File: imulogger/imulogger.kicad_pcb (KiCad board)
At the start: 2 copper layers, 64 x 25 mm, 36 parts, among them J1 DEBUG, J2 BATCONN, J4 Micro_SD_Card, J5 PWRCONN, Q1 TP0610T, U1 ESP32-WROOM-32, U2 USFS, U3 MCP1826S, U4 MCP73831-2-OT, U5 dw01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

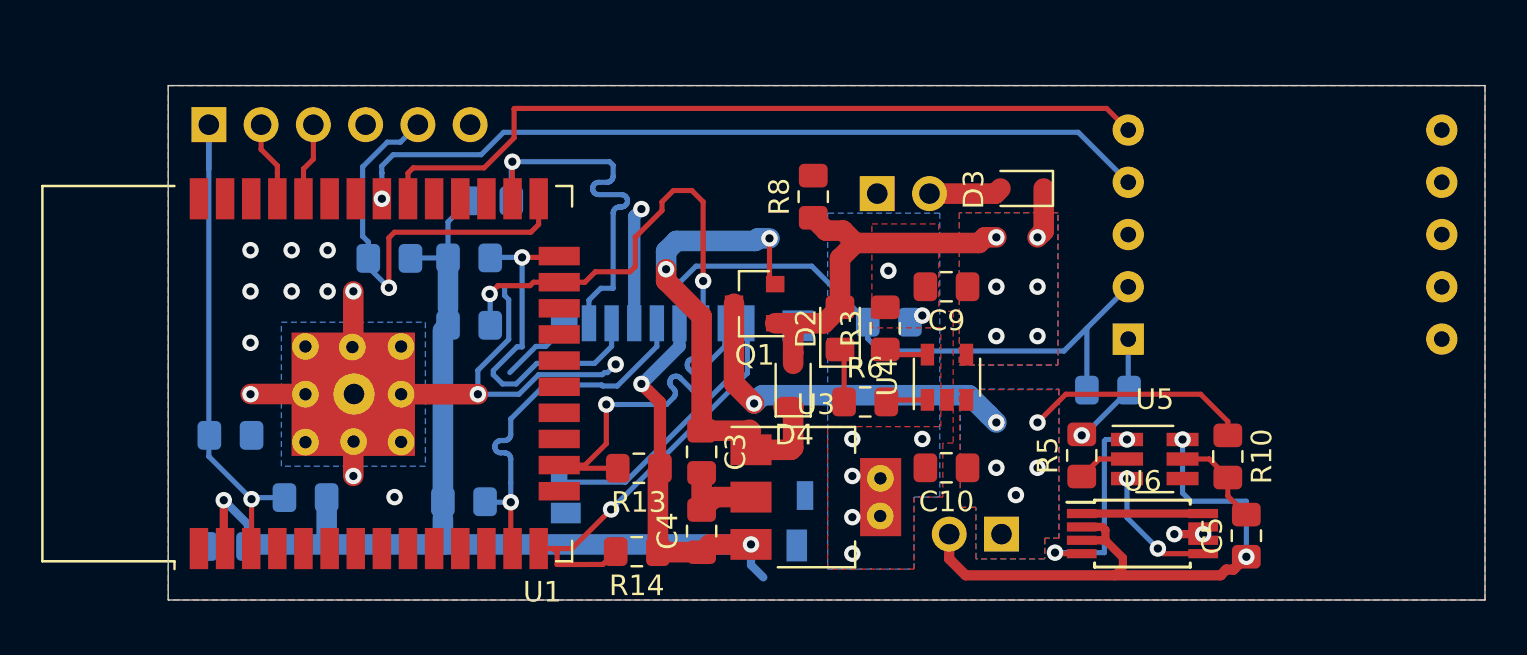
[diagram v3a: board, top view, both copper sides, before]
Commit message: imulogger: put connectors on the component side and remove useless track
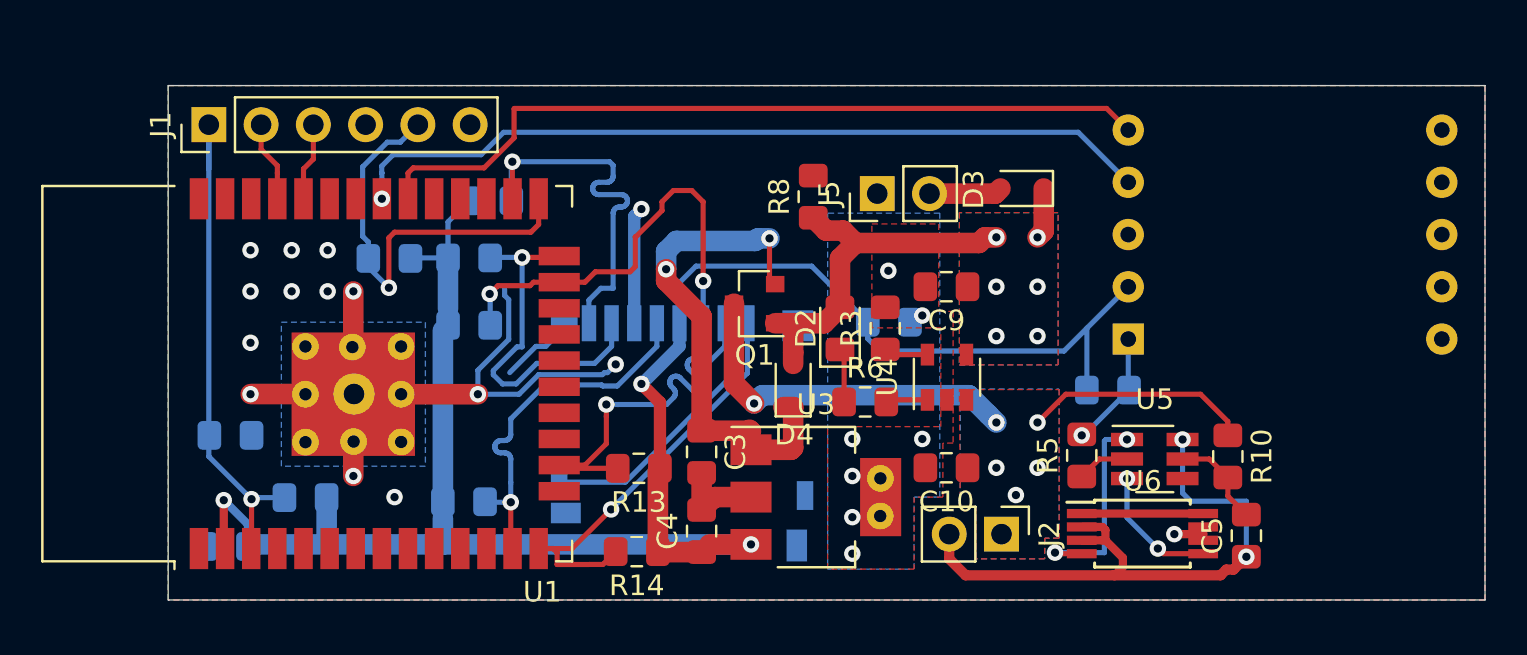
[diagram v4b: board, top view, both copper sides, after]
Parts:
- J1, J2, J5: moved to F.Cu
- turned J1 to 90 degrees
- turned J2 to 270 degrees
- turned J5 to 90 degrees
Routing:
- net +3V3: track 100.6 -> 98.8 mm
- net GND: vias 24 -> 23

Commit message: remove charger and add switch and JST socket
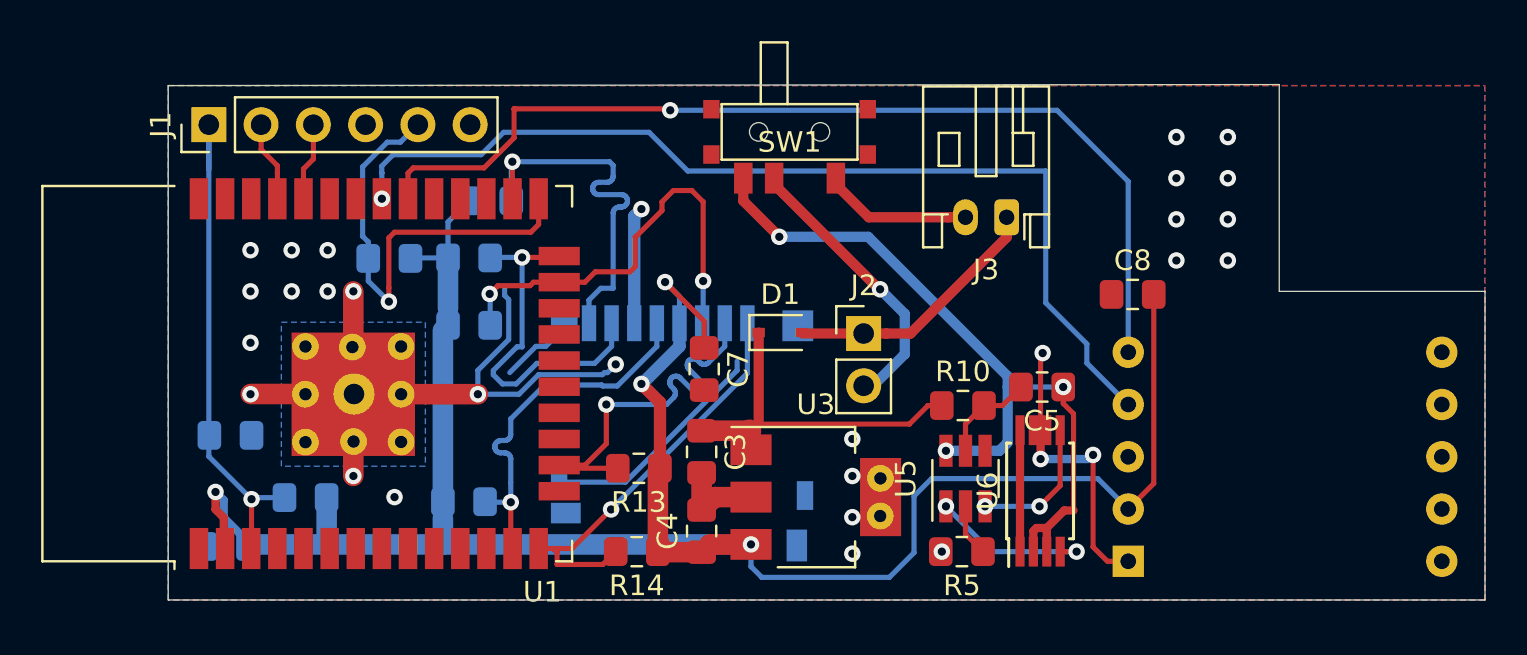
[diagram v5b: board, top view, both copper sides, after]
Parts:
- removed C10, C9: 4.7u, Capacitor_SMD:C_0805_2012Metric_Pad1.15x1.40mm_HandSolder
- removed D2: LED, LED_SMD:LED_0805_2012Metric_Pad1.15x1.40mm_HandSolder
- removed D3, D4: BAT20J, Diode_SMD:D_SOD-323
- removed J5: PWRCONN, Connector_PinHeader_2.54mm:PinHeader_1x02_P2.54mm_Vertical
- removed Q1: TP0610T, Package_TO_SOT_SMD:SOT-23
- removed R3: 2k, Resistor_SMD:R_0805_2012Metric_Pad1.15x1.40mm_HandSolder
- removed R6: 470, Resistor_SMD:R_0805_2012Metric_Pad1.15x1.40mm_HandSolder
- removed R8: 10k, Resistor_SMD:R_0805_2012Metric_Pad1.15x1.40mm_HandSolder
- removed U4: MCP73831-2-OT, Package_TO_SOT_SMD:SOT-23-5
- added D1: BAT20J, Diode_SMD:D_SOD-323, F.Cu at (149.8, 71.0)
- added J3: CHGCONN, Connector_JST:JST_PH_S2B-PH-K_1x02_P2.00mm_Horizontal, F.Cu at (160.8, 65.4)
- added SW1: SW_SPDT, imulogger-footprints:SK-3296S-01-L3, F.Cu at (150.2, 61.2)
- C7, C8: moved to F.Cu
- moved R10 13.1 mm to (158.6, 74.5), turned to 0 degrees
- moved C5 12.3 mm to (162.5, 73.7), turned to 180 degrees
- moved J2 11.8 mm to (153.8, 71.0), turned to 0 degrees
- moved U2 10.8 mm to (174.3, 77.0)
- moved C7 9.26 mm to (146.1, 72.8), turned to 270 degrees
- moved U5 9.25 mm to (158.8, 78.1), turned to 90 degrees
- moved R5 7.47 mm to (158.6, 81.7), turned to 180 degrees
- moved U6 5.39 mm to (162.4, 78.7), turned to 90 degrees
- moved C8 4.80 mm to (166.9, 69.2), turned to 0 degrees
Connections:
- C3 pad 1: Net-(C3-Pad1) -> V_BAT
- J2 pad 1: V_BAT -> Net-(D1-Pad2)
- J2 pad 2: Net-(C5-Pad1) -> Net-(J2-Pad2)
- U3 pad 1: Net-(C3-Pad1) -> V_BAT
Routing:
- net Net-(C3-Pad1): track 25.7 -> 0.00 mm, vias 2 -> 0
- net V_EXT: track 20.9 -> 0.00 mm, vias 6 -> 0
- net Net-(J2-Pad2): track 0.00 -> 13.8 mm, vias 0 -> 1
- net Net-(D1-Pad2): track 0.00 -> 12.9 mm
- net +3V3: track 98.8 -> 110.4 mm, vias 3 -> 4
- net V_BAT: track 28.8 -> 18.8 mm, vias 6 -> 0
- net IMU_SDA: track 38.8 -> 48.2 mm, vias 0 -> 1
- net IMU_SCL: track 39.6 -> 48.3 mm
- net GND: track 69.5 -> 76.7 mm, vias 23 -> 30
- net Net-(J3-Pad2): track 0.00 -> 7.26 mm
- net Net-(C5-Pad1): track 30.6 -> 37.3 mm, vias 2 -> 3
- net Net-(D3-Pad2): track 3.55 -> 0.00 mm
- net Net-(D2-Pad1): track 2.63 -> 0.00 mm
- net Net-(U5-Pad1): track 10.3 -> 8.06 mm
- net Net-(R3-Pad1): track 2.15 -> 0.00 mm
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- removed copper zone on B.Cu, net V_BAT
- removed copper zone on F.Cu, net V_BAT
- removed copper zone on B.Cu, net V_EXT
- removed copper zone on F.Cu, net V_EXT
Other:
- outline, holes or cut-outs redrawn

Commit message: remove battery protection circuit
my battery has that already and even if I had one without one
it'd be easier to buy one and glue it to the battery than soldering
these small ICs.
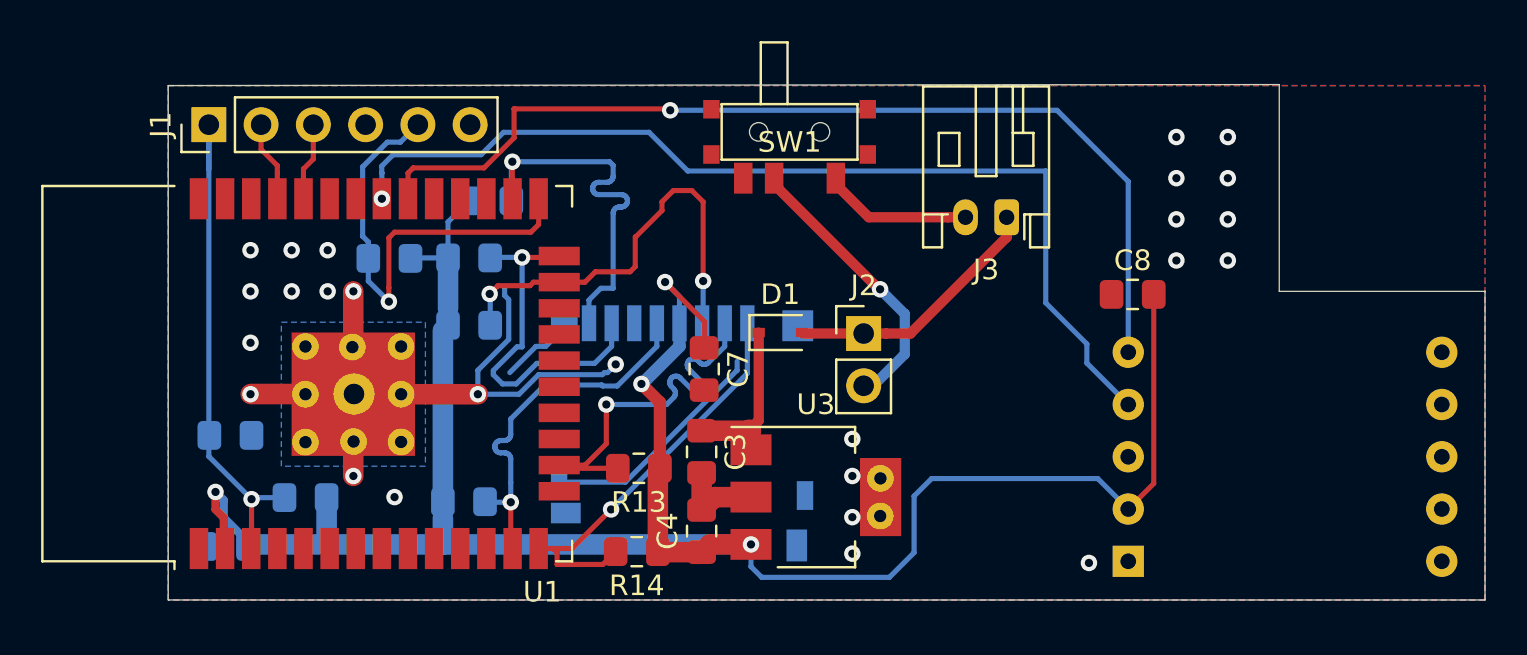
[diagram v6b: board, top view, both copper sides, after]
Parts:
- removed C5: 100n, Capacitor_SMD:C_0805_2012Metric_Pad1.15x1.40mm_HandSolder
- removed R10: 100, Resistor_SMD:R_0805_2012Metric_Pad1.15x1.40mm_HandSolder
- removed R5: 2K, Resistor_SMD:R_0805_2012Metric_Pad1.15x1.40mm_HandSolder
- removed U5: dw01, Package_TO_SOT_SMD:SOT-23-6_Handsoldering
- removed U6: FS8205A, Package_SO:TSSOP-8_4.4x3mm_P0.65mm
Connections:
- SW1 pad 3: Net-(C5-Pad1) -> GND
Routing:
- net Net-(C5-Pad1): track 37.3 -> 0.00 mm, vias 3 -> 0
- net GND: track 76.7 -> 56.0 mm, vias 30 -> 26
- net V_BAT: track 18.8 -> 9.04 mm
- net Net-(U5-Pad1): track 8.06 -> 0.00 mm, vias 2 -> 0
- net Net-(U5-Pad3): track 6.76 -> 0.00 mm, vias 2 -> 0
- net Net-(U6-Pad1): track 5.90 -> 0.00 mm
- net Net-(C5-Pad2): track 4.75 -> 0.00 mm
- net Net-(R5-Pad1): track 2.55 -> 0.00 mm
